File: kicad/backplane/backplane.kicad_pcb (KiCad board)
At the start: 2 copper layers, 302 x 104 mm, 24 parts, among them J1 Conn_02x30_Counter_Clockwise, J2 Conn_02x30_Counter_Clockwise, J3 Conn_02x30_Counter_Clockwise, J4 Conn_02x30_Counter_Clockwise, J5 Conn_02x30_Counter_Clockwise, J6 Conn_02x30_Counter_Clockwise, J7 Conn_02x30_Counter_Clockwise, J8 Conn_02x30_Counter_Clockwise

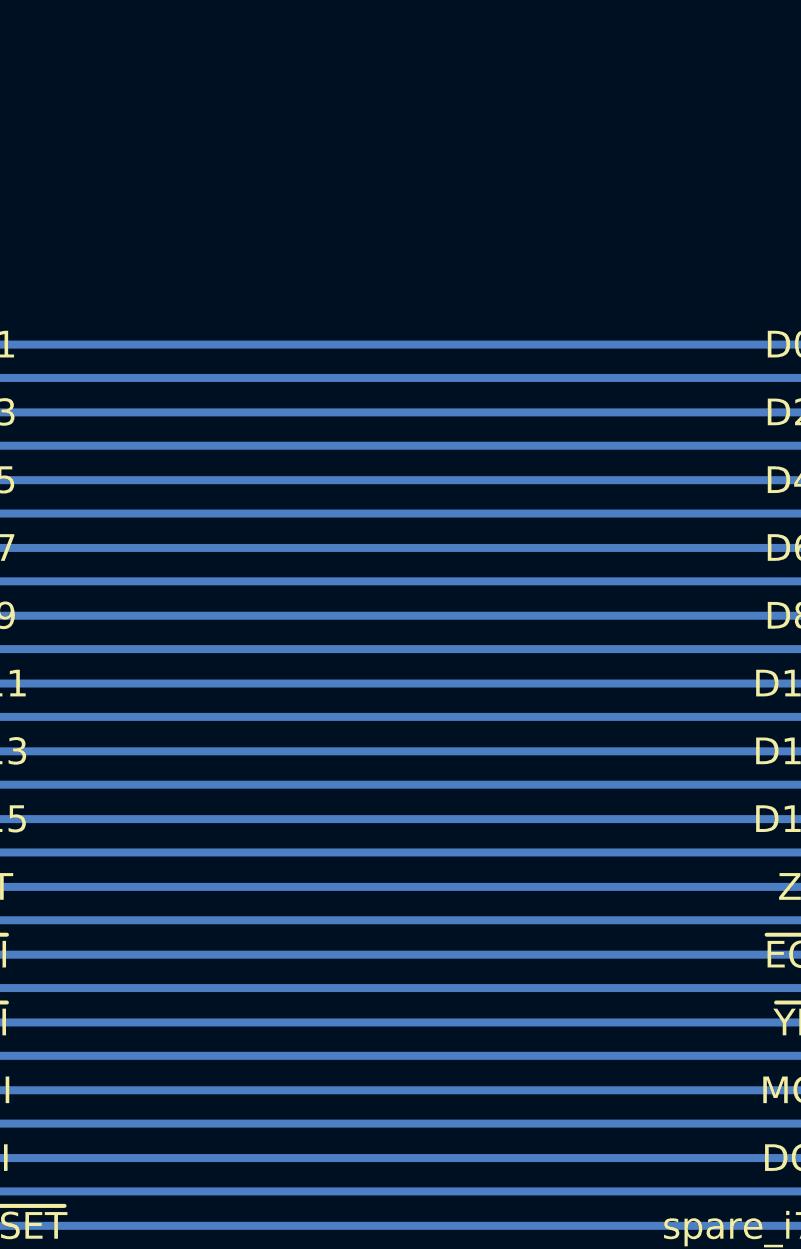
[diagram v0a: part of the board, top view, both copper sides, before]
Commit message: Seek faster, cut edges slower
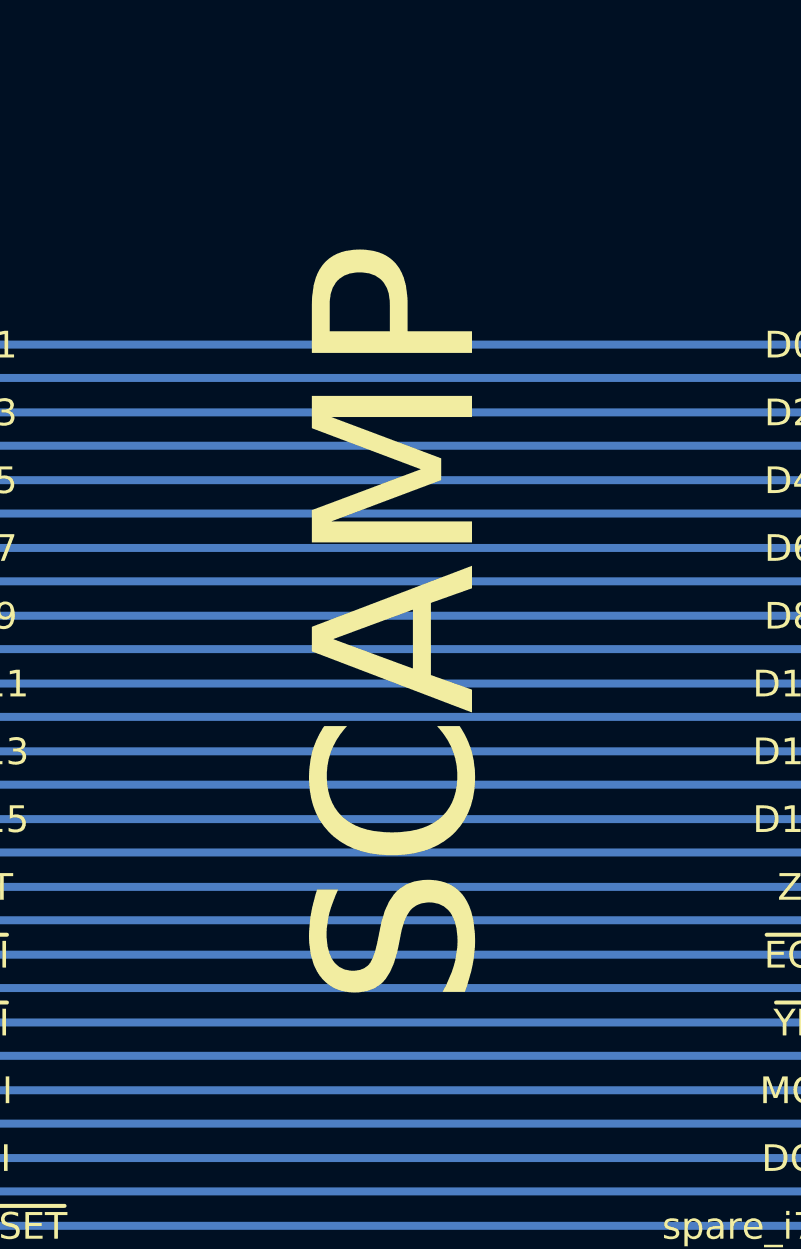
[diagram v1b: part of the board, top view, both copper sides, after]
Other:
- board text added: "SCAMP"

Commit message: Make backplane card suitable as a prototyping card
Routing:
- net D1: track 287.2 -> 579.2 mm
- net A13: track 287.2 -> 574.5 mm
- net spare_o7: track 287.2 -> 574.5 mm
- net Z: track 287.2 -> 574.5 mm
- net A4: track 287.2 -> 574.5 mm
- net D3: track 287.2 -> 574.5 mm
- net ~XI~: track 287.2 -> 574.5 mm
- net ~RESET~: track 287.2 -> 574.5 mm
- net ~AI~: track 287.2 -> 574.5 mm
- net unused: track 287.2 -> 574.5 mm
- net spare_o4: track 287.2 -> 574.5 mm
- net spare_U1: track 287.2 -> 574.5 mm
- net VCC: track 287.2 -> 574.5 mm
- net U0: track 287.2 -> 574.5 mm
- net NO: track 287.2 -> 574.5 mm
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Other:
- board size 302 x 104 mm -> 295 x 102.8 mm
